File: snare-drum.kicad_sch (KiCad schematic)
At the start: 85 parts, among them J1 Conn_02x05_Odd_Even, J2 GATE, J3 ACCENT_CV, J4 PITCH_CV, J5 SNAPPY_CV, J6 OUT, Q1 BCM857, Q2 BCM847, Q3 BC547, Q4 BCM847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

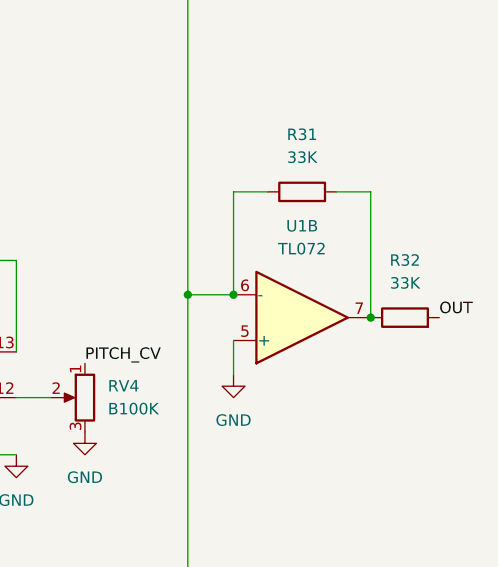
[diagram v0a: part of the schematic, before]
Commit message: fix resistor values
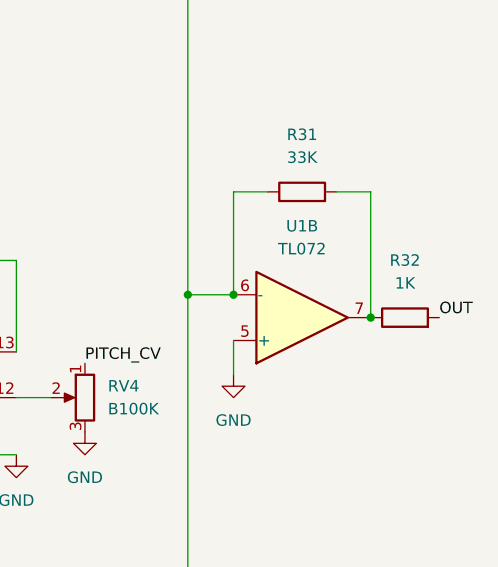
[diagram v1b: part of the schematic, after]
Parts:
- R32: value 33K -> 1K
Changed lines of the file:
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@@
       (effects (font (size 1.27 1.27)))
     )
-    (property "Value" "33K" (at 274.32 71.12 90)
+    (property "Value" "1K" (at 274.32 71.12 90)
       (effects (font (size 1.27 1.27)))
     )

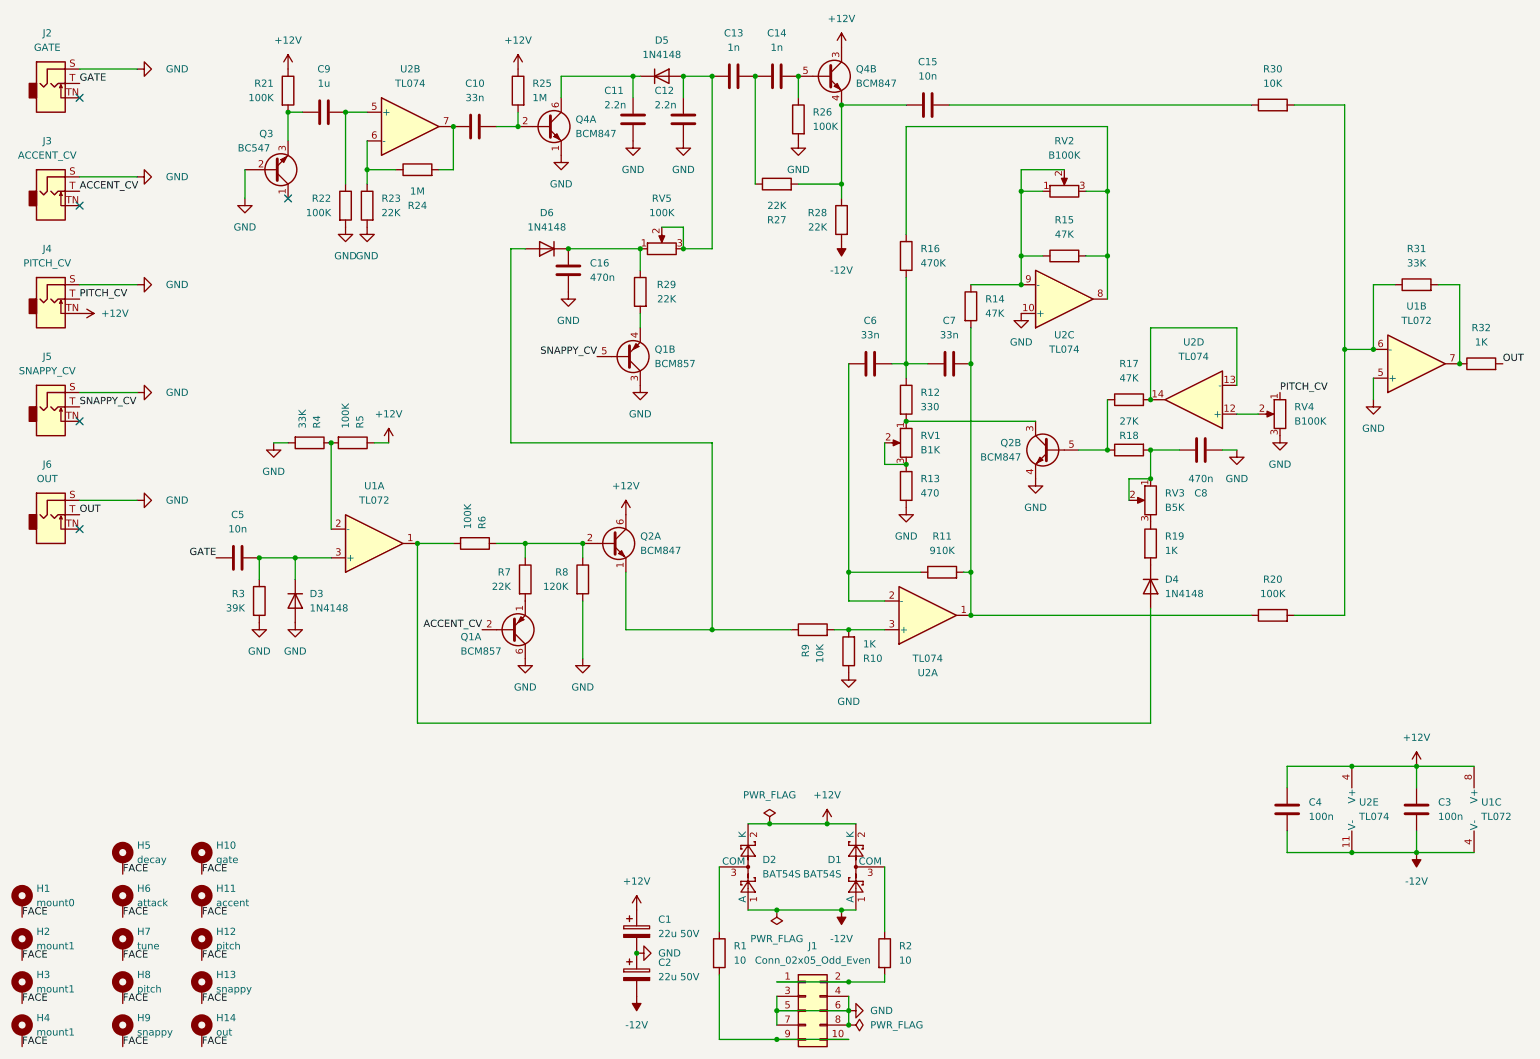
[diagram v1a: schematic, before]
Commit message: adding protection to CV inputs
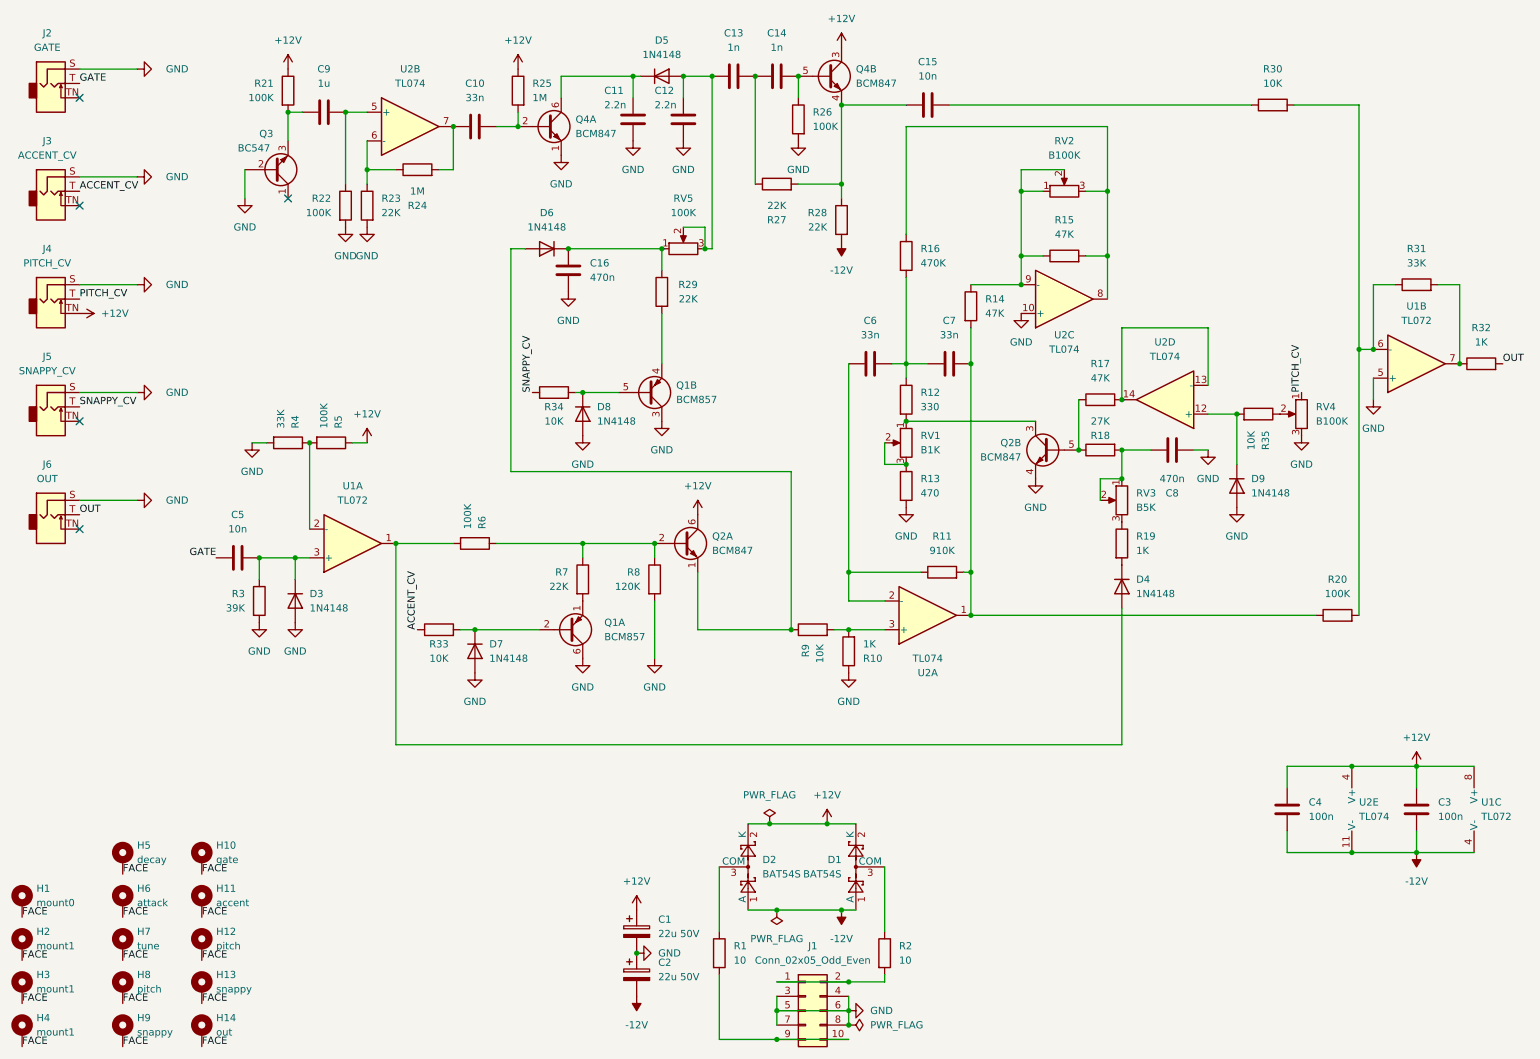
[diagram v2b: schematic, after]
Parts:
- added D7, D8, D9: 1N4148, Diode_SMD:D_SOD-323_HandSoldering, symbol Device:D
- added R33, R34, R35: 10K, Resistor_SMD:R_0805_2012Metric, symbol Device:R
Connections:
- net ACCENT_CV: now also R33.1; no longer Q1.2 (B1)
- net GND: now also D7.2 (A), D8.2 (A), D9.2 (A)
- net SNAPPY_CV: now also R34.1; no longer Q1.5 (B2)
- net at U2.12 (+): now also D9.1 (K), R35.2; no longer RV4.2
- new net: D7.1 (K), Q1.2 (B1), R33.2
- new net: D8.1 (K), Q1.5 (B2), R34.2
- new net: R35.1, RV4.2
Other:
- moved on the sheet: C8, D4, Q1A, Q1B, Q2A, R17, R18, R19, R20, R29, R4, R5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

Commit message: kicad 10, fixing bom
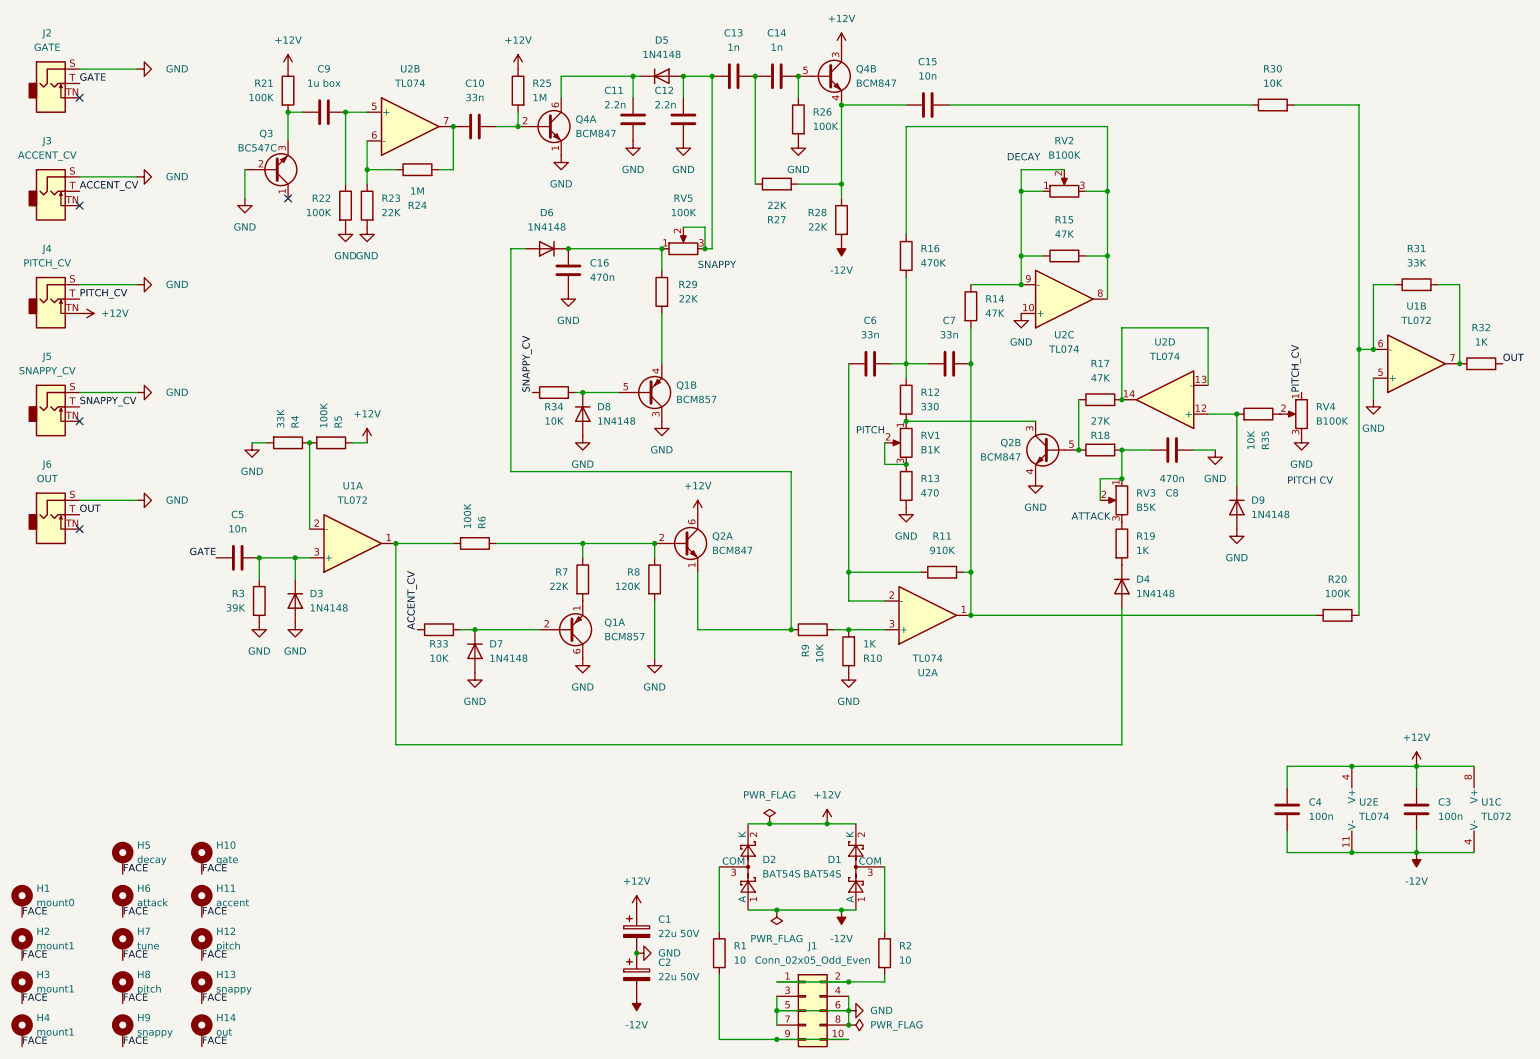
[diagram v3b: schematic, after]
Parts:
- C16, C8: footprint Capacitor_THT:C_Rect_L7.2mm_W5.5mm_P5.00mm_FKS2_FKP2_MKS2_MKP2 -> Capacitor_SMD:C_0805_2012Metric
- C9: value 1u -> 1u box
- Q3: value BC547 -> BC547C
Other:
- note added: "ATTACK"
- note added: "DECAY"
- note added: "PITCH"
- note added: "PITCH CV"
- note added: "SNAPPY"
- moved on the sheet: D9

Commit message: v0 ready
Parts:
- H7: value tune -> pitch
- H8: value pitch -> snappy
- H9: value snappy -> pitch cv
- RV4: value B100K -> 100K; footprint Eurorack:Potentiometer_RV16AF-41-15R1 -> Potentiometer_THT:Potentiometer_Bourns_3296W_Vertical
- RV5: value 100K -> B100K; footprint Potentiometer_THT:Potentiometer_Bourns_3296W_Vertical -> Eurorack:Potentiometer_RV16AF-41-15R1
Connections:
- net +12V: no longer J4.TN
- net GND: now also RV4.1; no longer RV4.3
- net PITCH_CV: now also RV4.3; no longer RV4.1
- net at C16.1, D6.1 (K), R29.1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: now also RV5.2
- net at R14.1, R15.1, RV2.2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: now also RV2.3; no longer RV2.1
- net at C12.1, C13.1, D5.2 (A)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: no longer RV5.2
- net at R13.1, RV1.2: now also RV1.1; no longer RV1.3
- net at R15.2, R16.1, U2.8: now also RV2.1; no longer RV2.3
- net at Q2.3 (C2), R12.2: now also RV1.3; no longer RV1.1
- no-connect marks 5 -> 6
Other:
- moved on the sheet: C1, C2, RV1, RV2, RV4
